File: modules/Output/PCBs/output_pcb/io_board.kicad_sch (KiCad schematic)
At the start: 11 parts, among them J1 THONKICONN, J2 THONKICONN, U1 TL072

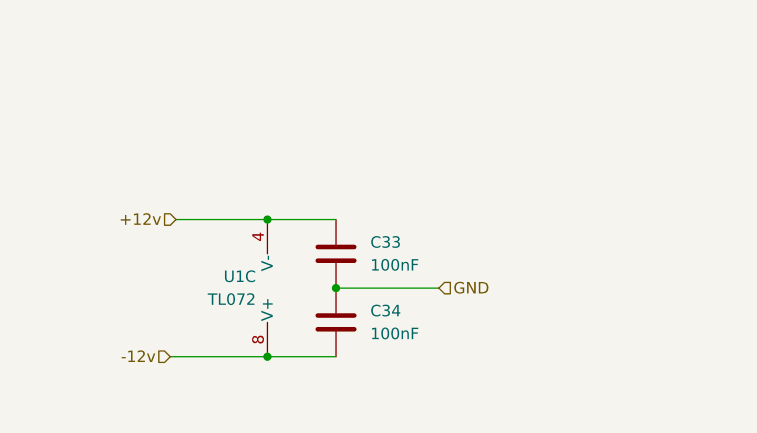
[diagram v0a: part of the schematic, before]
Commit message: finish output PCB
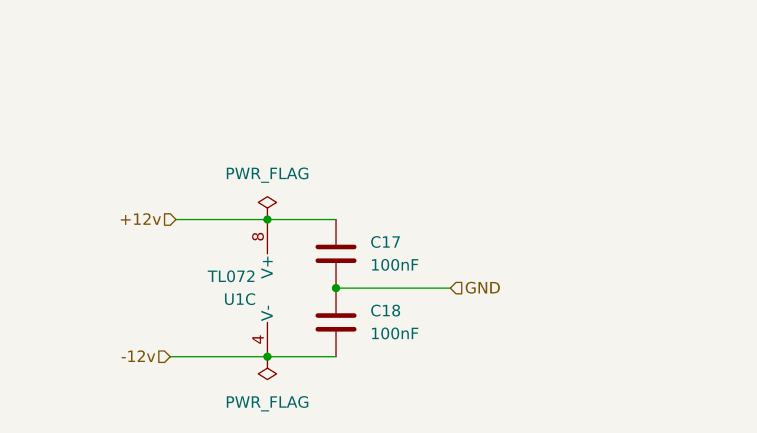
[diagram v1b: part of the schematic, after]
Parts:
- C17: renamed from C33; footprint (none) -> Capacitor_THT:C_Disc_D4.7mm_W2.5mm_P5.00mm
- C18: renamed from C34; footprint (none) -> Capacitor_THT:C_Disc_D4.7mm_W2.5mm_P5.00mm
- U1: footprint (none) -> Package_DIP:DIP-8_W7.62mm
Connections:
- net +12v: now also U1.8 (V+); no longer U1.4 (V-)
- net -12v: now also U1.4 (V-); no longer U1.8 (V+)
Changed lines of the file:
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@@
+    (stroke (width 0) (type default))
+  )
+  (wire (pts (xy 52.705 154.94) (xy 63.5 154.94))
     (stroke (width 0) (type default))
   )
@@
     (stroke (width 0) (type default))
   )
-  (wire (pts (xy 52.705 154.94) (xy 63.5 154.94))
-    (stroke (width 0) (type default))
-  )
   (wire (pts (xy 137.16 73.66) (xy 168.91 73.66))
     (stroke (width 0) (type default))
@@
     (stroke (width 0) (type default))
   )
-  (wire (pts (xy 71.12 147.32) (xy 82.55 147.32))
+  (wire (pts (xy 71.12 147.32) (xy 83.82 147.32))
     (stroke (width 0) (type default))
   )
@@
     (effects (font (size 1.27 1.27)) (justify right))
   )
-  (hierarchical_label "GND" (shape input) (at 82.55 147.32 0) (fields_autoplaced)
+  (hierarchical_label "GND" (shape input) (at 83.82 147.32 0) (fields_autoplaced)
     (effects (font (size 1.27 1.27)) (justify left))
   )
@@
     (effects (font (size 1.27 1.27)) (justify right))
   )
+  (netclass_flag "" (length 2.54) (shape round) (at 54.61 154.94 0) (fields_autoplaced)
+    (effects (font (size 1.27 1.27)) (justify left bottom))
+    (property "Netclass" "Power" (at 55.3085 152.4 0)
+      (effects (font (size 1.27 1.27) italic) (justify left))
+    )
+  )
+  (netclass_flag "" (length 2.54) (shape round) (at 54.61 139.7 0) (fields_autoplaced)
+    (effects (font (size 1.27 1.27)) (justify left bottom))
+    (property "Netclass" "Power" (at 55.3085 137.16 0)
+      (effects (font (size 1.27 1.27) italic) (justify left))
+    )
+  )
+  (netclass_flag "" (length 2.54) (shape round) (at 82.55 147.32 0) (fields_autoplaced)
+    (effects (font (size 1.27 1.27)) (justify left bottom))
+    (property "Netclass" "Power" (at 83.2485 144.78 0)
+      (effects (font (size 1.27 1.27) italic) (justify left))
+    )
+  )
   (symbol (lib_id "FreeModular:THONKICONN") (at 43.18 78.74 0) (unit 1)
     (in_bom yes) (on_board yes) (dnp no) (fields_autoplaced)
@@
     )
   )
-  (symbol (lib_id "Amplifier_Operational:TL072") (at 66.04 147.32 0) (mirror x) (unit 3)
-    (in_bom yes) (on_board yes) (dnp no) (fields_autoplaced)
-    (property "Reference" "U1" (at 62.23 146.05 0)
+  (symbol (lib_id "Amplifier_Operational:TL072") (at 66.04 147.32 0) (unit 3)
+    (in_bom yes) (on_board yes) (dnp no)
+    (property "Reference" "U1" (at 62.23 148.59 0)
       (effects (font (size 1.27 1.27)) (justify right))
     )
-    (property "Value" "TL072" (at 62.23 148.59 0)
+    (property "Value" "TL072" (at 62.23 146.05 0)
       (effects (font (size 1.27 1.27)) (justify right))
     )
-    (property "Footprint" "" (at 66.04 147.32 0)
+    (property "Footprint" "Package_DIP:DIP-8_W7.62mm" (at 66.04 147.32 0)
       (effects (font (size 1.27 1.27)) hide)
     )
@@
       (effects (font (size 1.27 1.27)))
     )
-    (property "Footprint" "" (at 93.98 96.52 0)
+    (property "Footprint" "Package_DIP:DIP-8_W7.62mm" (at 93.98 96.52 0)
       (effects (font (size 1.27 1.27)) hide)
     )
@@
   (symbol (lib_id "Device:C") (at 71.12 151.13 0) (unit 1)
     (in_bom yes) (on_board yes) (dnp no) (fields_autoplaced)
-    (property "Reference" "C34" (at 74.93 149.86 0)
+    (property "Reference" "C18" (at 74.93 149.86 0)
       (effects (font (size 1.27 1.27)) (justify left))
     )
@@
       (effects (font (size 1.27 1.27)) (justify left))
     )
-    (property "Footprint" "" (at 72.0852 154.94 0)
+    (property "Footprint" "Capacitor_THT:C_Disc_D4.7mm_W2.5mm_P5.00mm" (at 72.0852 154.94 0)
       (effects (font (size 1.27 1.27)) hide)
     )
@@
       (project "output_pcb"
         (path "/9afe4d4d-3155-44ea-9484-068db54e495a/56a0a3f0-f4aa-41c8-a222-11ae39b02663"
-          (reference "C34") (unit 1)
+          (reference "C18") (unit 1)
         )
       )
@@
     )
   )
+  (symbol (lib_id "power:PWR_FLAG") (at 63.5 139.7 0) (unit 1)
+    (in_bom yes) (on_board yes) (dnp no) (fields_autoplaced)
+    (property "Reference" "#FLG04" (at 63.5 137.795 0)
+      (effects (font (size 1.27 1.27)) hide)
+    )
+    (property "Value" "PWR_FLAG" (at 63.5 134.62 0)
+      (effects (font (size 1.27 1.27)))
+    )
+    (property "Footprint" "" (at 63.5 139.7 0)
+      (effects (font (size 1.27 1.27)) hide)
+    )
+    (property "Datasheet" "~" (at 63.5 139.7 0)
+      (effects (font (size 1.27 1.27)) hide)
+    )
+    (pin "1")
+    (instances
+      (project "output_pcb"
+        (path "/9afe4d4d-3155-44ea-9484-068db54e495a/56a0a3f0-f4aa-41c8-a222-11ae39b02663"
+          (reference "#FLG04") (unit 1)
+        )
+      )
+    )
+  )
   (symbol (lib_id "Amplifier_Operational:TL072") (at 93.98 73.66 0) (mirror x) (unit 1)
     (in_bom yes) (on_board yes) (dnp no)
@@
       (effects (font (size 1.27 1.27)))
     )
-    (property "Footprint" "" (at 93.98 73.66 0)
+    (property "Footprint" "Package_DIP:DIP-8_W7.62mm" (at 93.98 73.66 0)
       (effects (font (size 1.27 1.27)) hide)
     )
@@
     )
   )
+  (symbol (lib_id "power:PWR_FLAG") (at 63.5 154.94 0) (mirror x) (unit 1)
+    (in_bom yes) (on_board yes) (dnp no)
+    (property "Reference" "#FLG03" (at 63.5 156.845 0)
+      (effects (font (size 1.27 1.27)) hide)
+    )
+    (property "Value" "PWR_FLAG" (at 63.5 160.02 0)
+      (effects (font (size 1.27 1.27)))
+    )
+    (property "Footprint" "" (at 63.5 154.94 0)
+      (effects (font (size 1.27 1.27)) hide)
+    )
+    (property "Datasheet" "~" (at 63.5 154.94 0)
+      (effects (font (size 1.27 1.27)) hide)
+    )
+    (pin "1")
+    (instances
+      (project "output_pcb"
+        (path "/9afe4d4d-3155-44ea-9484-068db54e495a/56a0a3f0-f4aa-41c8-a222-11ae39b02663"
+          (reference "#FLG03") (unit 1)
+        )
+      )
+    )
+  )
   (symbol (lib_id "Device:C") (at 71.12 143.51 0) (unit 1)
     (in_bom yes) (on_board yes) (dnp no) (fields_autoplaced)
-    (property "Reference" "C33" (at 74.93 142.24 0)
+    (property "Reference" "C17" (at 74.93 142.24 0)
       (effects (font (size 1.27 1.27)) (justify left))
     )
@@
       (effects (font (size 1.27 1.27)) (justify left))
     )
-    (property "Footprint" "" (at 72.0852 147.32 0)
+    (property "Footprint" "Capacitor_THT:C_Disc_D4.7mm_W2.5mm_P5.00mm" (at 72.0852 147.32 0)
       (effects (font (size 1.27 1.27)) hide)
     )
@@
       (project "output_pcb"
         (path "/9afe4d4d-3155-44ea-9484-068db54e495a/56a0a3f0-f4aa-41c8-a222-11ae39b02663"
-          (reference "C33") (unit 1)
-        )
-      )
+          (reference "C17") (unit 1)
+        )
+      )

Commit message: fix polarity mismatch bugs in output pcb
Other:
- company: (none) -> Free Modular
- title: (none) -> Output
